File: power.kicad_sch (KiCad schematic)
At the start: 21 parts, among them J401 Barrel_Jack_MountingPin, Q401 PMOS, U401 TLV76733, U402 LMR33620CQ5

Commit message: Split schematic into three subprojects
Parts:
- renumbered C401 to C18, C402 to C19, C403 to C20, C404 to C21, C405 to C22, C406 to C23, C407 to C24, C408 to C25, C409 to C26, D401 to D2, D402 to D3, D403 to D4, F401 to F1, J401 to J10, L401 to L2, L402 to L3, Q401 to Q1, R401 to R6, R402 to R7, U401 to U2, U402 to U3

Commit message: Added annotations and missing footprints
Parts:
- J10: footprint (none) -> Connector_BarrelJack:BarrelJack_Horizontal
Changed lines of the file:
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@@
       (effects (font (size 1.27 1.27)))
     )
-    (property "Footprint" "" (at 66.04 130.556 0)
+    (property "Footprint" "Connector_BarrelJack:BarrelJack_Horizontal" (at 66.04 130.556 0)
       (effects (font (size 1.27 1.27)) hide)
     )

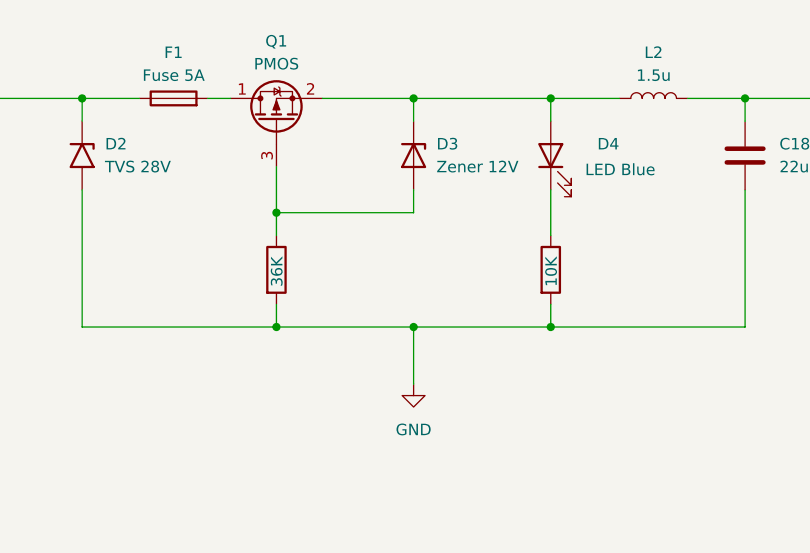
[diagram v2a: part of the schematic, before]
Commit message: Updated designators positions
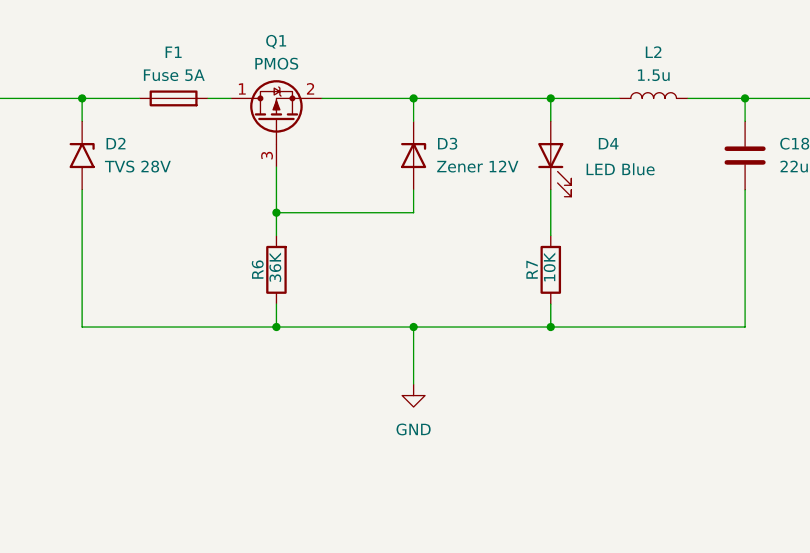
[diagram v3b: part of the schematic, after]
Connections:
- net GND: now also R6.1, R7.1; no longer R6.2, R7.2
- net at D4.1 (K): now also R7.2; no longer R7.1
- net at D3.2 (A), Q1.3 (G): now also R6.2; no longer R6.1
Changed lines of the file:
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@@
     )
   )
-  (symbol (lib_id "Device:R") (at 92.71 72.39 0) (unit 1)
+  (symbol (lib_id "Device:R") (at 92.71 72.39 180) (unit 1)
     (in_bom yes) (on_board yes) (dnp no)
-    (property "Reference" "R6" (at 95.25 71.12 0)
-      (effects (font (size 1.27 1.27)) (justify left) hide)
+    (property "Reference" "R6" (at 90.678 72.39 90)
+      (effects (font (size 1.27 1.27)))
     )
-    (property "Value" "36K" (at 92.7847 74.2813 90)
+    (property "Value" "36K" (at 92.6353 70.4987 90)
       (effects (font (size 1.27 1.27)) (justify left))
     )
-    (property "Footprint" "Resistor_SMD:R_0603_1608Metric_Pad0.98x0.95mm_HandSolder" (at 90.932 72.39 90)
+    (property "Footprint" "Resistor_SMD:R_0603_1608Metric_Pad0.98x0.95mm_HandSolder" (at 94.488 72.39 90)
       (effects (font (size 1.27 1.27)) hide)
     )
@@
     )
   )
-  (symbol (lib_id "Device:R") (at 123.19 72.39 0) (unit 1)
+  (symbol (lib_id "Device:R") (at 123.19 72.39 180) (unit 1)
     (in_bom yes) (on_board yes) (dnp no)
-    (property "Reference" "R7" (at 125.73 71.12 0)
-      (effects (font (size 1.27 1.27)) (justify left) hide)
+    (property "Reference" "R7" (at 121.158 72.39 90)
+      (effects (font (size 1.27 1.27)))
     )
-    (property "Value" "10K" (at 123.2705 74.2813 90)
+    (property "Value" "10K" (at 123.1095 70.4987 90)
       (effects (font (size 1.27 1.27)) (justify left))
     )
-    (property "Footprint" "Resistor_SMD:R_0603_1608Metric_Pad0.98x0.95mm_HandSolder" (at 121.412 72.39 90)
+    (property "Footprint" "Resistor_SMD:R_0603_1608Metric_Pad0.98x0.95mm_HandSolder" (at 124.968 72.39 90)
       (effects (font (size 1.27 1.27)) hide)
     )

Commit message: Set capacitor and resistor values on tranciever circuits
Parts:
- C18, C22, C23: value 22u -> 22uF
- C19, C20, C26: value 1u -> 1uF
- C21: value 100n -> 100nF
- C24: value 10u -> 10uF
- C25: value 220n -> 220nF
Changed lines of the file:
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@@
       (effects (font (size 1.27 1.27)) (justify left))
     )
-    (property "Value" "1u" (at 207.01 62.23 0)
+    (property "Value" "1uF" (at 207.01 62.23 0)
       (effects (font (size 1.27 1.27)) (justify left))
     )
@@
       (effects (font (size 1.27 1.27)) hide)
     )
-    (property "Datasheet" "~" (at 203.2 60.96 0)
+    (property "Datasheet" "1uF 50V X7R 10%" (at 203.2 60.96 0)
       (effects (font (size 1.27 1.27)) hide)
     )
@@
       (effects (font (size 1.27 1.27)) (justify left))
     )
-    (property "Value" "22u" (at 233.68 124.46 0)
+    (property "Value" "22uF" (at 233.68 124.46 0)
       (effects (font (size 1.27 1.27)) (justify left))
     )
@@
       (effects (font (size 1.27 1.27)) hide)
     )
-    (property "Datasheet" "~" (at 229.87 123.19 0)
+    (property "Datasheet" "22uF 50V X5R 10%" (at 229.87 123.19 0)
       (effects (font (size 1.27 1.27)) hide)
     )
@@
       (effects (font (size 1.27 1.27)) (justify left))
     )
-    (property "Value" "10u" (at 147.32 138.43 0)
+    (property "Value" "10uF" (at 147.32 138.43 0)
       (effects (font (size 1.27 1.27)) (justify left))
     )
@@
       (effects (font (size 1.27 1.27)) hide)
     )
-    (property "Datasheet" "~" (at 143.51 137.16 0)
+    (property "Datasheet" "10uF 50V X5R 10%" (at 143.51 137.16 0)
       (effects (font (size 1.27 1.27)) hide)
     )
@@
       (effects (font (size 1.27 1.27)) (justify left))
     )
-    (property "Value" "1u" (at 172.72 143.51 0)
+    (property "Value" "1uF" (at 172.72 143.51 0)
       (effects (font (size 1.27 1.27)) (justify left))
     )
@@
       (effects (font (size 1.27 1.27)) hide)
     )
-    (property "Datasheet" "~" (at 168.91 142.24 0)
+    (property "Datasheet" "1uF 50V X7R 10%" (at 168.91 142.24 0)
       (effects (font (size 1.27 1.27)) hide)
     )
@@
       (effects (font (size 1.27 1.27)) (justify left))
     )
-    (property "Value" "1u" (at 242.57 62.23 0)
+    (property "Value" "1uF" (at 242.57 62.23 0)
       (effects (font (size 1.27 1.27)) (justify left))
     )
@@
       (effects (font (size 1.27 1.27)) hide)
     )
-    (property "Datasheet" "~" (at 238.76 60.96 0)
+    (property "Datasheet" "1uF 50V X7R 10%" (at 238.76 60.96 0)
       (effects (font (size 1.27 1.27)) hide)
     )
@@
       (effects (font (size 1.27 1.27)) (justify left))
     )
-    (property "Value" "22u" (at 246.38 124.46 0)
+    (property "Value" "22uF" (at 246.38 124.46 0)
       (effects (font (size 1.27 1.27)) (justify left))
     )
@@
       (effects (font (size 1.27 1.27)) hide)
     )
-    (property "Datasheet" "~" (at 242.57 123.19 0)
+    (property "Datasheet" "22uF 50V X5R 10%" (at 242.57 123.19 0)
       (effects (font (size 1.27 1.27)) hide)
     )
@@
       (effects (font (size 1.27 1.27)) hide)
     )
-    (property "Datasheet" "~" (at 92.71 72.39 0)
+    (property "Datasheet" "36kΩ 75V Thick Film 1%" (at 92.71 72.39 0)
       (effects (font (size 1.27 1.27)) hide)
     )
@@
       (effects (font (size 1.27 1.27)) hide)
     )
-    (property "Datasheet" "~" (at 123.19 72.39 0)
+    (property "Datasheet" "10kΩ 75V Thick Film 1%" (at 123.19 72.39 0)
       (effects (font (size 1.27 1.27)) hide)
     )
@@
       (effects (font (size 1.27 1.27)) (justify left))
     )
-    (property "Value" "220n" (at 160.02 138.43 0)
+    (property "Value" "220nF" (at 160.02 138.43 0)
       (effects (font (size 1.27 1.27)) (justify left))
     )
@@
       (effects (font (size 1.27 1.27)) hide)
     )
-    (property "Datasheet" "~" (at 156.21 137.16 0)
+    (property "Datasheet" "220nF 50V X7R 10%" (at 156.21 137.16 0)
       (effects (font (size 1.27 1.27)) hide)
     )
@@
       (effects (font (size 1.27 1.27)) (justify left))
     )
-    (property "Value" "22u" (at 148.59 60.96 0)
+    (property "Value" "22uF" (at 148.59 60.96 0)
       (effects (font (size 1.27 1.27)) (justify left))
     )
@@
       (effects (font (size 1.27 1.27)) hide)
     )
-    (property "Datasheet" "~" (at 144.78 59.69 0)
+    (property "Datasheet" "22uF 50V X5R 10%" (at 144.78 59.69 0)
       (effects (font (size 1.27 1.27)) hide)
     )
@@
       (effects (font (size 1.27 1.27)))
     )
-    (property "Value" "100n" (at 200.66 110.49 90)
+    (property "Value" "100nF" (at 200.66 110.49 90)
       (effects (font (size 1.27 1.27)))
     )
@@
       (effects (font (size 1.27 1.27)) hide)
     )
-    (property "Datasheet" "~" (at 200.66 115.57 0)
-      (effects (font (size 1.27 1.27)) hide)
-    )
+    (property "Datasheet" "100nF 50V X7R 10%" (at 200.66 115.57 0)
+      (effects (font (size 1.27 1.27)) hide)
+    )

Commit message: Assigned footprints for digital components
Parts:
- F1: footprint Fuse:Fuse_1812_4532Metric_Pad1.30x3.40mm_HandSolder -> Fuse:Fuse_2920_7451Metric_Pad2.10x5.45mm_HandSolder
- J10: value Barrel_Jack_MountingPin -> DC Barrel Jack
- L2, L3: value 1.5u -> 1.5uH; footprint Inductor_SMD:L_Bourns-SRN4018 -> Inductor_SMD_Wurth:L_Wurth_WE-LQSH-4020
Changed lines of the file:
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@@
       (effects (font (size 1.27 1.27)) hide)
     )
-    (property "Datasheet" "~" (at 123.19 59.69 0)
+    (property "Datasheet" "https://www.lcsc.com/product-detail/C2288.html" (at 123.19 59.69 0)
       (effects (font (size 1.27 1.27)) hide)
     )
@@
       (effects (font (size 1.27 1.27)))
     )
-    (property "Value" "Barrel_Jack_MountingPin" (at 64.77 123.19 0)
+    (property "Value" "DC Barrel Jack" (at 64.77 123.19 0)
       (effects (font (size 1.27 1.27)))
     )
@@
       (effects (font (size 1.27 1.27)))
     )
-    (property "Footprint" "Fuse:Fuse_1812_4532Metric_Pad1.30x3.40mm_HandSolder" (at 81.28 55.118 90)
-      (effects (font (size 1.27 1.27)) hide)
-    )
-    (property "Datasheet" "~" (at 81.28 53.34 0)
+    (property "Footprint" "Fuse:Fuse_2920_7451Metric_Pad2.10x5.45mm_HandSolder" (at 81.28 55.118 90)
+      (effects (font (size 1.27 1.27)) hide)
+    )
+    (property "Datasheet" "https://www.lcsc.com/product-detail/C19078762.html" (at 81.28 53.34 0)
       (effects (font (size 1.27 1.27)) hide)
     )
@@
       (effects (font (size 1.27 1.27)))
     )
-    (property "Value" "1.5u" (at 134.62 50.8 90)
-      (effects (font (size 1.27 1.27)))
-    )
-    (property "Footprint" "Inductor_SMD:L_Bourns-SRN4018" (at 134.62 53.34 0)
+    (property "Value" "1.5uH" (at 134.62 50.8 90)
+      (effects (font (size 1.27 1.27)))
+    )
+    (property "Footprint" "Inductor_SMD_Wurth:L_Wurth_WE-LQSH-4020" (at 134.62 53.34 0)
       (effects (font (size 1.27 1.27)) hide)
     )
@@
       (effects (font (size 1.27 1.27)) hide)
     )
-    (property "Datasheet" "" (at 181.61 134.62 0)
+    (property "Datasheet" "https://www.lcsc.com/product-detail/C5219383.html" (at 181.61 134.62 0)
       (effects (font (size 1.27 1.27)) hide)
     )
@@
       (effects (font (size 1.27 1.27)) hide)
     )
-    (property "Datasheet" "" (at 219.71 55.88 0)
+    (property "Datasheet" "https://www.lcsc.com/product-detail/C2848334.html" (at 219.71 55.88 0)
       (effects (font (size 1.27 1.27)) hide)
     )
@@
       (effects (font (size 1.27 1.27)) hide)
     )
-    (property "Datasheet" "~" (at 107.95 59.69 0)
+    (property "Datasheet" "https://www.lcsc.com/product-detail/C108437.html" (at 107.95 59.69 0)
       (effects (font (size 1.27 1.27)) hide)
     )
@@
       (effects (font (size 1.27 1.27)) hide)
     )
-    (property "Datasheet" "~" (at 71.12 58.42 0)
+    (property "Datasheet" "https://www.lcsc.com/product-detail/C148227.html" (at 71.12 58.42 0)
       (effects (font (size 1.27 1.27)) hide)
     )
@@
       (effects (font (size 1.27 1.27)))
     )
-    (property "Value" "1.5u" (at 213.36 113.03 90)
-      (effects (font (size 1.27 1.27)))
-    )
-    (property "Footprint" "Inductor_SMD:L_Bourns-SRN4018" (at 213.36 115.57 0)
-      (effects (font (size 1.27 1.27)) hide)
-    )
+    (property "Value" "1.5uH" (at 213.36 113.03 90)
+      (effects (font (size 1.27 1.27)))
+    )
+    (property "Footprint" "Inductor_SMD_Wurth:L_Wurth_WE-LQSH-4020" (at 213.36 115.57 0)
+      (effects (font (size 1.27 1.27)) hide)
+    )

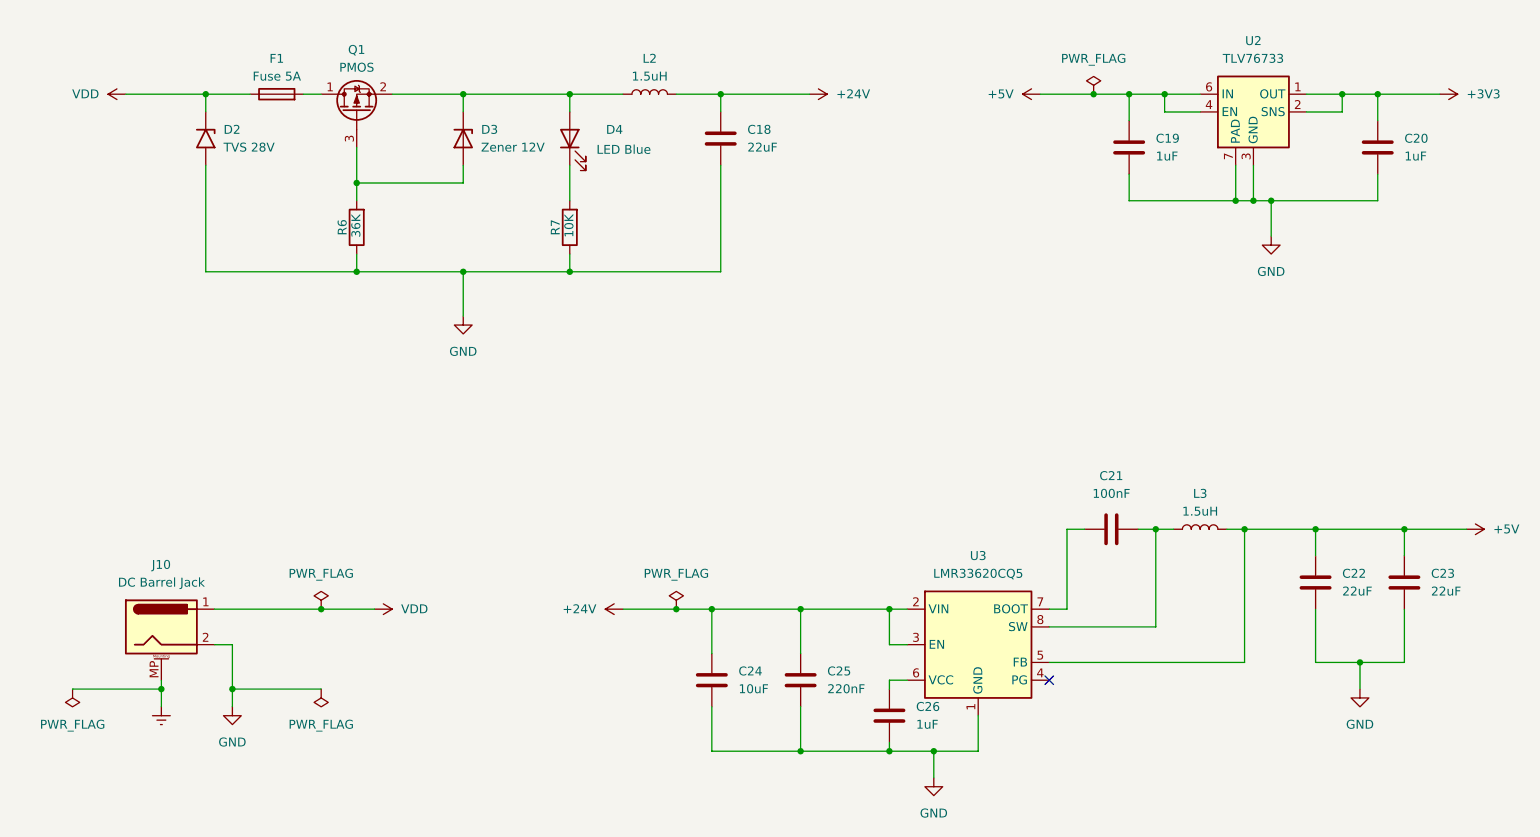
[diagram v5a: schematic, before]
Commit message: Redone power input circuit
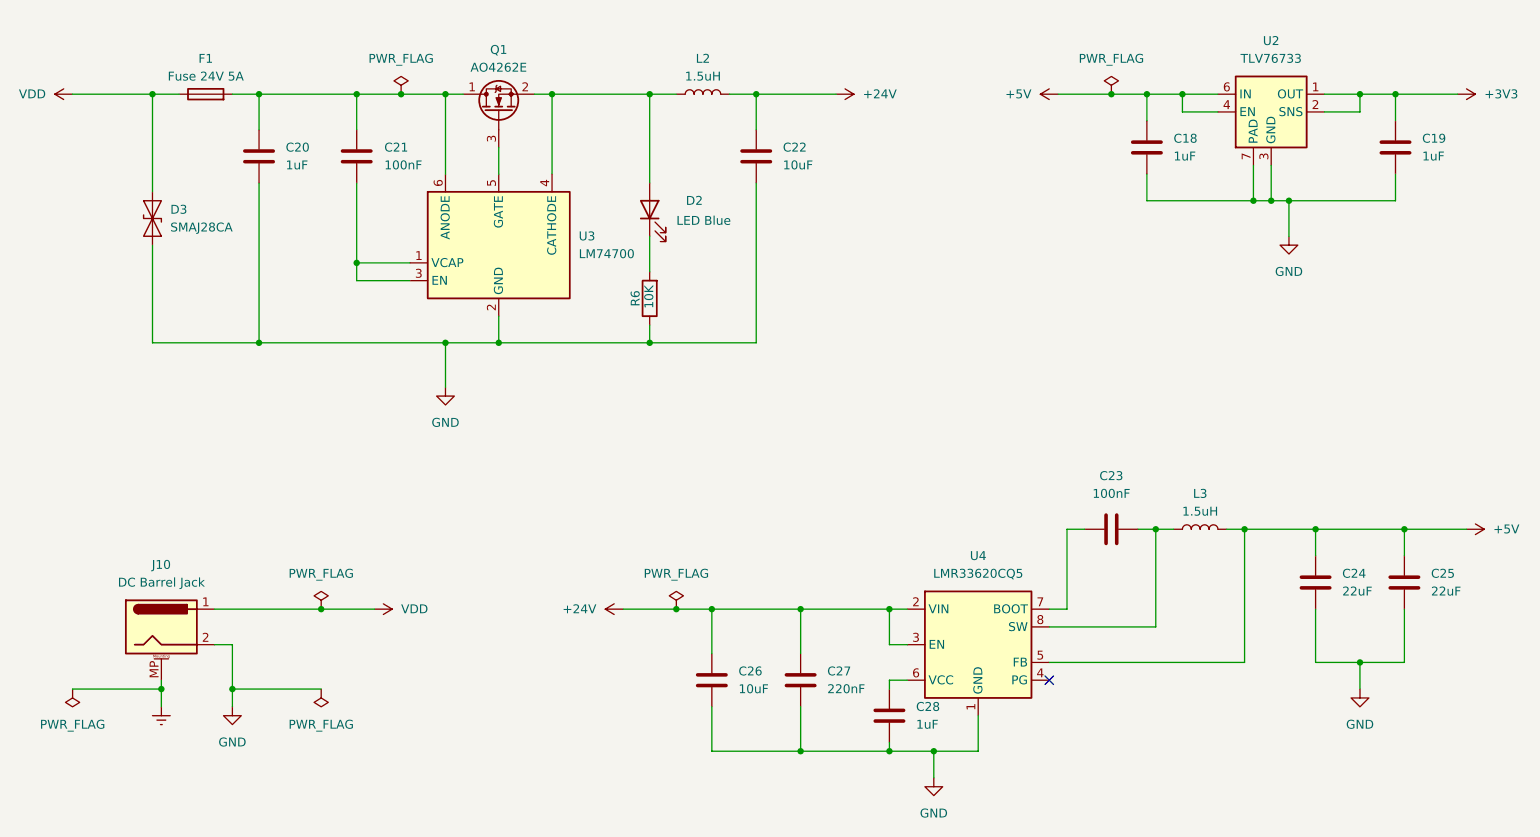
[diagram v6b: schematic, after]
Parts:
- removed D2: TVS 28V, Diode_SMD:D_SMA, symbol Diode:SMAJ28A
- removed D3: Zener 12V, Package_TO_SOT_SMD:SOT-23, symbol Device:D_Zener
- removed Q1: PMOS, Package_DFN_QFN:DFN-8-1EP_6x5mm_P1.27mm_EP4x4mm, symbol Device:Q_PMOS_DSG
- removed R6: 36K, Resistor_SMD:R_0603_1608Metric_Pad0.98x0.95mm_HandSolder, symbol Device:R
- removed U3: LMR33620CQ5, Package_SO:Texas_HSOP-8-1EP_3.9x4.9mm_P1.27mm_ThermalVias, symbol Regulator_Switching:LMR33620ADDA
- added C20: 1uF, Capacitor_SMD:C_0805_2012Metric_Pad1.18x1.45mm_HandSolder, symbol Device:C
- added C21: 100nF, Capacitor_SMD:C_0603_1608Metric_Pad1.08x0.95mm_HandSolder, symbol Device:C
- added D3: SMAJ28CA, Diode_SMD:D_SMA, symbol Diode:SMAJ28CA
- added Q1: AO4262E, Package_SO:SOIC-8_3.9x4.9mm_P1.27mm, symbol Device:Q_NMOS_DSG
- added U3: LM74700, Package_TO_SOT_SMD:SOT-23-6, symbol Power_Management:LM74700
- added U4: LMR33620CQ5, Package_SO:Texas_HSOP-8-1EP_3.9x4.9mm_P1.27mm_ThermalVias, symbol Regulator_Switching:LMR33620ADDA
- C22: renamed from C18; value 22uF -> 10uF
- F1: value Fuse 5A -> Fuse 24V 5A
- L2, L3: footprint Inductor_SMD_Wurth:L_Wurth_WE-LQSH-4020 -> Inductor_SMD:L_Bourns_SRP5030T
- renumbered C19 to C18, C20 to C19, C21 to C23, C22 to C24, C23 to C25, C24 to C26, C25 to C27, C26 to C28, D4 to D2, R7 to R6
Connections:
- net +24V: now also U4.2 (VIN), U4.3 (EN)
- net +5V: now also U4.5 (FB)
- net GND: now also C20.2, D3.1 (A1), U3.2 (GND), U4.1 (GND), U4.9 (GND)
- net VDD: now also D3.2 (A2)
- net at D2.2 (A), L2.1: now also Q1.2 (S), U3.4 (CATHODE)
- net at C28.1: now also U4.6 (VCC)
- net at F1.2: now also C20.1, C21.2, Q1.1 (D), U3.6 (ANODE)
- net at C23.1: now also U4.7 (BOOT)
- net at C23.2, L3.1: now also U4.8 (SW)
- new net: Q1.3 (G), U3.5 (GATE)
- new net: C21.1, U3.1 (VCAP), U3.3 (EN)
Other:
- moved on the sheet: C18, C19, C22, D2, F1, L2, R6, U2
